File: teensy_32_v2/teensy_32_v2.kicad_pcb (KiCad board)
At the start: 4 copper layers, 65 x 56.5 mm, 5 parts, among them P1 S9200-ND

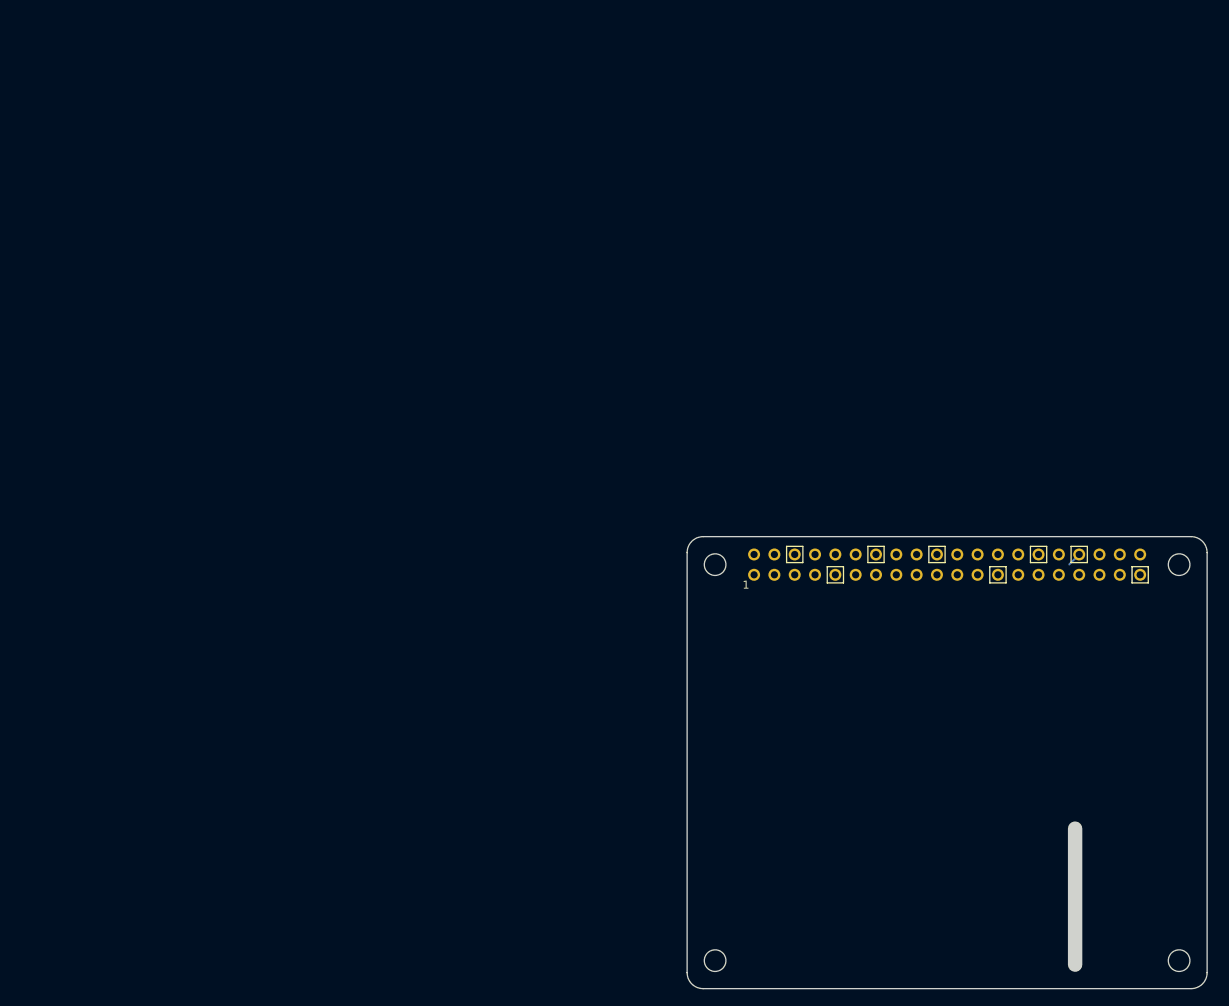
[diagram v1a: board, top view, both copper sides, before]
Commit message: another attempt at Hat layout -- pre routing
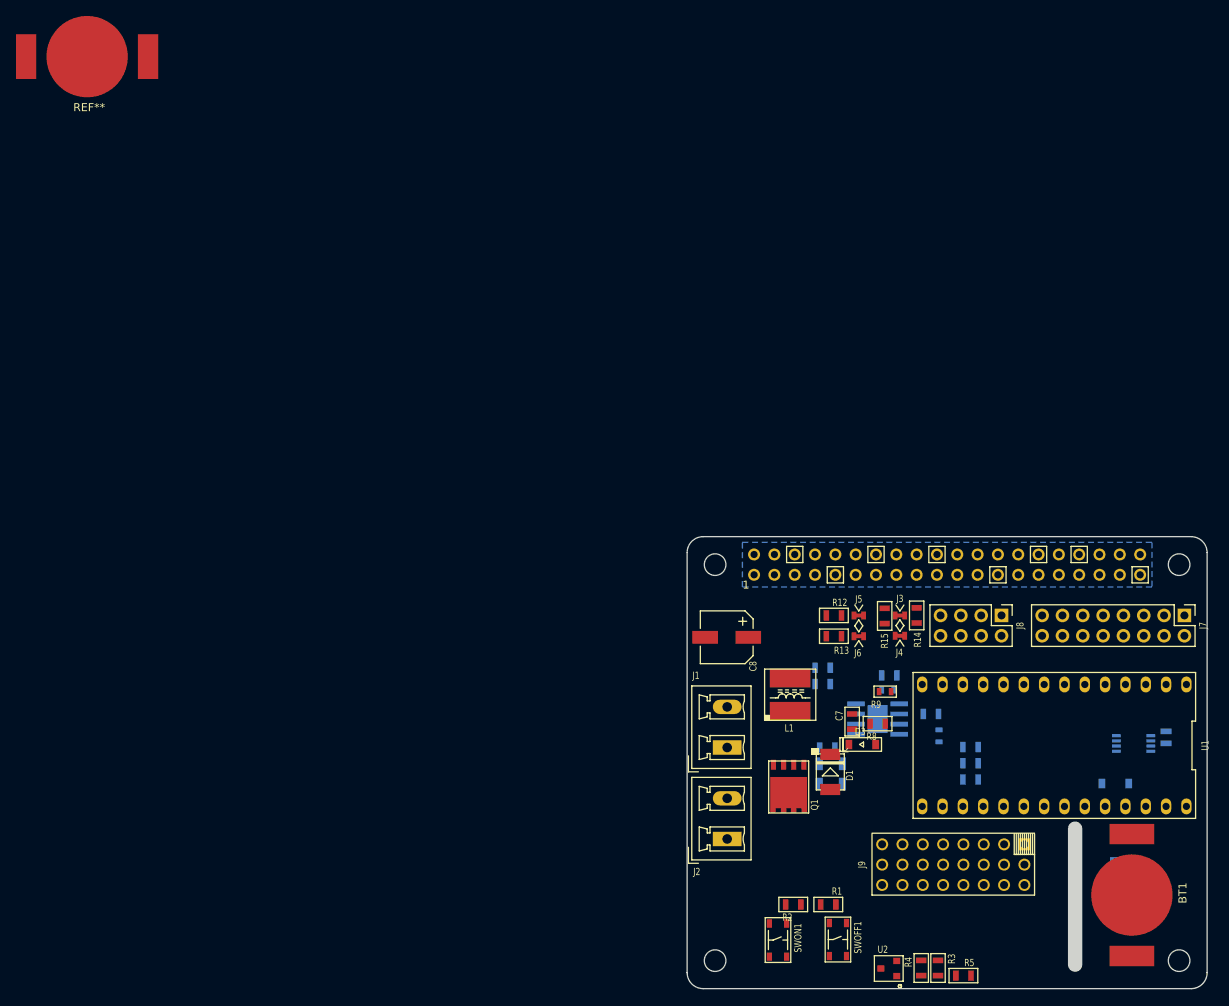
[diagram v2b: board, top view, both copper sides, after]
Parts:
- added BT1: BC-2009-ND, teensy:BC-2009-ND, F.Cu at (130.6, 104.8)
- added C1: MF-CAP-0805-0.1uF, MF_Passives:MF_Passives-C0805, B.Cu at (110.4, 88.3)
- added C10: CL21A226KOQNNNE, MF_Passives:MF_Passives-C0805, B.Cu at (91.9, 76.4)
- added C2: MF-CAP-0805-0.1uF, MF_Passives:MF_Passives-C0805, B.Cu at (92.5, 86.4)
- added C3: CL31A106MBHNNNE, MF_Passives:MF_Passives-C1206, B.Cu at (93.0, 90.9)
- added C4: CL31A106MBHNNNE, MF_Passives:MF_Passives-C1206, B.Cu at (93.0, 88.4)
- added C5: MF-CAP-0805-0.1uF, MF_Passives:MF_Passives-C0805, B.Cu at (100.3, 77.3)
- added C6: MF-CAP-0603-4.7nF, MF_Passives:MF_Passives-C0603, B.Cu at (106.5, 84.9)
- added C7: MF-CAP-0805-0.1uF, MF_Passives:MF_Passives-C0805, F.Cu at (95.6, 83.1)
- added C8: MF-CAP-6.3MM-100uF, MF_Passives:MF_Passives-CP6.3MM, F.Cu at (79.9, 72.6)
- added C9: CL21A226KOQNNNE, MF_Passives:MF_Passives-C0805, B.Cu at (91.9, 78.4)
- added D1: PMEG3050EP,115, teensy:SOD-128, F.Cu at (92.9, 89.4)
- added D2: BAT42, MF_Discrete_Semiconductor:MF_Discrete_Semiconductor-SOD-123, B.Cu at (128.5, 90.9)
- added D3: MF-DIO-SOD123-BAT42, MF_Discrete_Semiconductor:MF_Discrete_Semiconductor-SOD-123, F.Cu at (96.9, 86.0)
- added D4: BAT42, MF_Discrete_Semiconductor:MF_Discrete_Semiconductor-SOD-123, B.Cu at (128.5, 98.8)
- added J1: 277-1667-ND, Connectors_Phoenix:PhoenixContact_MCV-G_02x5.08mm_Vertical, F.Cu at (80.0, 86.4)
- added J2: 277-1667-ND, Connectors_Phoenix:PhoenixContact_MCV-G_02x5.08mm_Vertical, F.Cu at (80.0, 97.8)
- added J3: CJ, teensy:CJ-2, F.Cu at (101.6, 69.8)
- added J4: CJ, teensy:CJ-2, F.Cu at (101.6, 72.4)
- added J5: CJ, teensy:CJ-2, F.Cu at (96.5, 69.8)
- added J6: CJ, teensy:CJ-2, F.Cu at (96.5, 72.5)
- added J7: M20-9980845, Pin_Headers:Pin_Header_Straight_2x08_Pitch2.54mm, F.Cu at (137.2, 69.8)
- added J8: M20-9970445, Pin_Headers:Pin_Header_Straight_2x04_Pitch2.54mm, F.Cu at (114.3, 69.8)
- added J9: Drive, teensy:CONN_03x08, F.Cu at (107.0, 101.0)
- added L1: SRN6045TA-6R3M, teensy:SRN6045TA, F.Cu at (87.9, 79.8)
- added Q1: STL62P3LLH6, teensy:POWERFLAT_5x6, F.Cu at (87.7, 90.0)
- added R1: MF-RES-0805-15K, MF_Passives:MF_Passives-R0805, F.Cu at (92.6, 106.0)
- added R10: RC0603FR-0712KL, MF_Passives:MF_Passives-R0603, B.Cu at (100.1, 79.2)
- added R12: MF-RES-0603-2K, MF_Passives:MF_Passives-R0805, F.Cu at (93.3, 69.8)
- added R13: MF-RES-0603-2K, MF_Passives:MF_Passives-R0805, F.Cu at (93.3, 72.5)
- added R14: MF-RES-0603-2K, MF_Passives:MF_Passives-R0805, F.Cu at (103.7, 69.8)
- added R15: MF-RES-0603-2K, MF_Passives:MF_Passives-R0805, F.Cu at (99.7, 69.9)
- added R16: MF-RES-0805-15K, MF_Passives:MF_Passives-R0805, B.Cu at (105.5, 82.2)
- added R2: MF-RES-0604-2K, MF_Passives:MF_Passives-R0805, F.Cu at (88.3, 106.0)
- added R3: MF-RES-0805-100K, MF_Passives:MF_Passives-R0805, F.Cu at (106.4, 113.9)
- added R4: MF-RES-0805-100K, MF_Passives:MF_Passives-R0805, F.Cu at (104.3, 113.9)
- added R5: MF-RES-0604-2K, MF_Passives:MF_Passives-R0805, F.Cu at (109.5, 114.9)
- added R6: MF-RES-0805-470K, MF_Passives:MF_Passives-R0805, B.Cu at (110.4, 90.4)
- added R7: MF-RES-0805-100K, MF_Passives:MF_Passives-R0805, B.Cu at (110.4, 86.3)
- added R8: MF-RES-0805-100K, MF_Passives:MF_Passives-R0805, F.Cu at (98.8, 83.4)
- added R9: RC0603FR-0763K4L, MF_Passives:MF_Passives-R0603, F.Cu at (99.8, 79.4)
- added REF**: BC-2009-ND, BC-2009-ND, F.Cu at (0.00, 0.00)
- added SWOFF1: MF-SW-TACT-4.2MM, MF_Switches:MF_Switches-TACT4.2MM, F.Cu at (93.9, 110.4)
- added SWON1: MF-SW-TACT-4.2MM, MF_Switches:MF_Switches-TACT4.2MM, F.Cu at (86.4, 110.4)
- added U1: TEENSY_3, teensy:TEENSY_3, F.Cu at (120.9, 86.1)
- added U2: MF-DSC-SOT233-BSS138, MF_Discrete_Semiconductor:MF_Discrete_Semiconductor-SOT-23-3, F.Cu at (100.2, 114.0)
- added U3: DS7257G, teensy:DS7257G, B.Cu at (98.8, 82.8)
- added U4: PCF8563TS/5,118, Housings_SSOP:TSSOP-8_3x3mm_Pitch0.65mm, B.Cu at (130.8, 85.9)
- added Y1: 32 kHz, teensy:SC-20S, B.Cu at (134.9, 85.1)
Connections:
- net +2V5 renamed +3V3
- net /R_12 renamed Net-(P1-Pad32)
- net /R_13 renamed Net-(P1-Pad33)
- net /R_16 renamed Net-(P1-Pad36)
- net /R_17 renamed Net-(P1-Pad11)
- net /R_18 renamed Net-(P1-Pad12)
- net /R_19 renamed Net-(P1-Pad35)
- net /R_20 renamed Net-(P1-Pad38)
- net /R_21 renamed Net-(P1-Pad40)
- net /R_22 renamed Net-(P1-Pad15)
- net /R_23 renamed Net-(P1-Pad16)
- net /R_24 renamed Net-(P1-Pad18)
- net /R_25 renamed Net-(P1-Pad22)
- net /R_26 renamed Net-(P1-Pad37)
- net /R_27 renamed Net-(P1-Pad13)
- net /R_4 renamed Net-(P1-Pad7)
- net /R_5 renamed Net-(P1-Pad29)
- net /R_6 renamed Net-(P1-Pad31)
- net /R_CE0 renamed Net-(P1-Pad24)
- net /R_CE1 renamed Net-(P1-Pad26)
- net /R_ID_SC renamed Net-(P1-Pad28)
- net /R_ID_SD renamed Net-(P1-Pad27)
- net /R_MISO renamed Net-(P1-Pad21)
- net /R_MOSI renamed Net-(P1-Pad19)
- net /R_SCK renamed Net-(P1-Pad23)
- P1 pad 10: /R_RXD -> /R_RX
- P1 pad 8: /R_TXD -> /R_TX
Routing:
- net GND: track 1.90 -> 0.00 mm
- added copper zone on B.Cu, net GND
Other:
- copper layers 4 -> 2
- net class Default: clearance 0.2 -> 0.13
- rule trace_clearance: 0.2 -> 0.13

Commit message: Macrofab proto order of teensy hat v2b
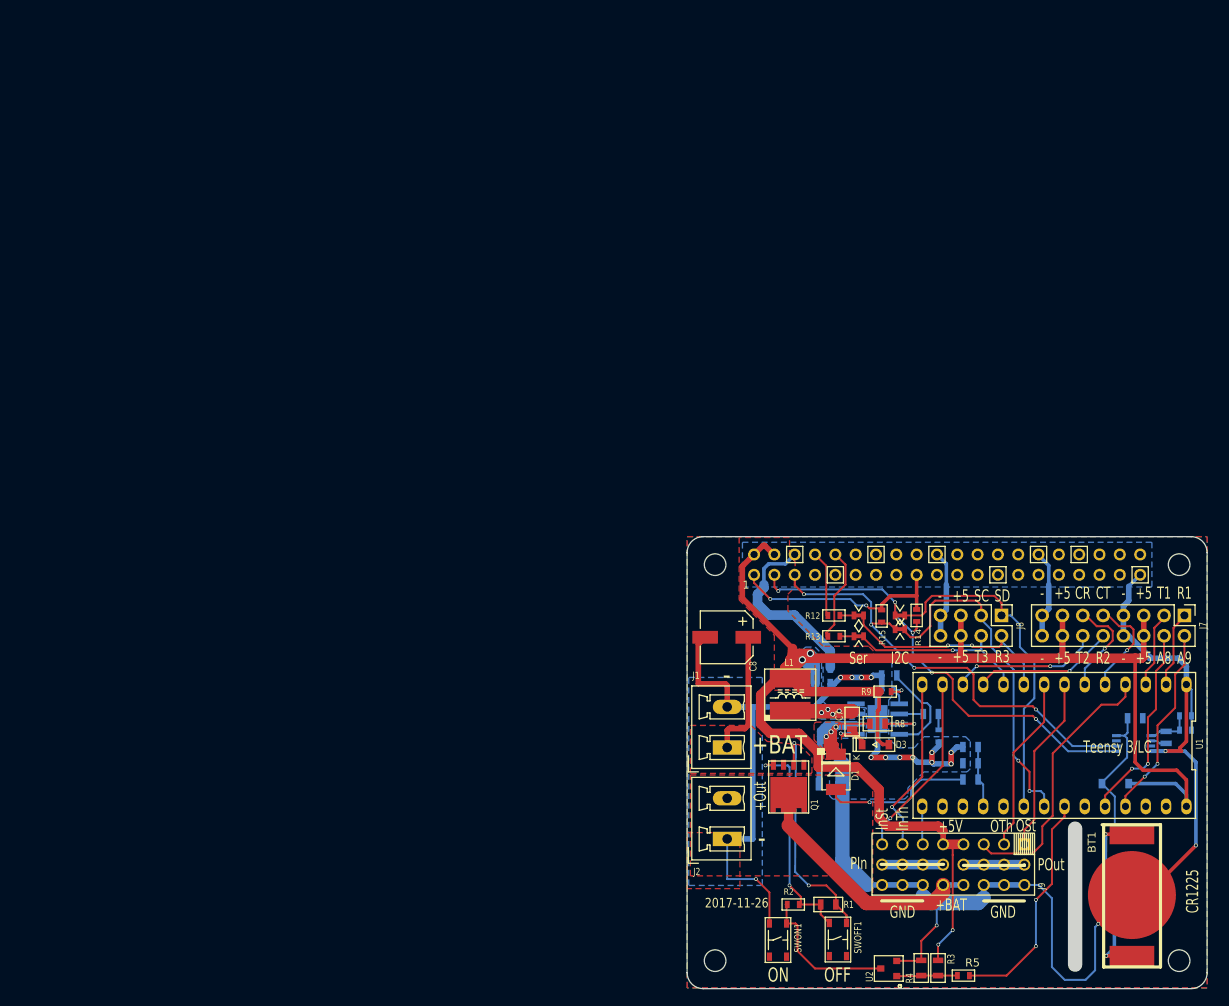
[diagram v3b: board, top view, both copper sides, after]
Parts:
- removed the REF** at (0.00, 0.00)
- added C11: MF-CAP-0805-0.1uF, MF_Passives:MF_Passives-C0805, B.Cu at (131.0, 82.7)
- added C12: MF-CAP-0603-4.7nF, MF_Passives:MF_Passives-C0603, B.Cu at (137.3, 82.4)
- added C13: MF-CAP-0603-4.7nF, MF_Passives:MF_Passives-C0603, B.Cu at (137.3, 84.2)
- R12, R13, R14, R15: footprint MF_Passives:MF_Passives-R0805 -> MF_Passives:MF_Passives-R0603
- R2, R5: value MF-RES-0604-2K -> MF-RES-0603-2K; footprint MF_Passives:MF_Passives-R0805 -> MF_Passives:MF_Passives-R0603
- Y1: value 32 kHz -> SC20S-12.5PF20PPM
- moved D3 1.65 mm to (98.6, 86.0)
- moved J4 0.83 mm to (101.6, 71.6)
- moved D1 0.70 mm to (93.6, 89.4)
- moved R15 0.38 mm to (99.3, 69.9)
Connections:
- net +BATT renamed +12V
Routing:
- net GND: track 0.00 -> 300.2 mm, vias 0 -> 17
- net +5V: track 0.00 -> 214.6 mm, vias 0 -> 4
- net /R_SDA: track 0.00 -> 60.0 mm, vias 0 -> 5
- net /R_SCL: track 0.00 -> 56.7 mm, vias 0 -> 4
- net +12V: track 0.00 -> 50.3 mm, vias 0 -> 1
- net /Power/VIN: track 0.00 -> 45.3 mm, vias 0 -> 2
- net /T_SCL: track 0.00 -> 43.0 mm, vias 0 -> 2
- net /T_SDA: track 0.00 -> 42.5 mm
- net /Power/V_SW: track 0.00 -> 41.8 mm, vias 0 -> 4
- net /Power/V_VIN: track 0.00 -> 34.5 mm, vias 0 -> 3
- net /OUT_AUX: track 0.00 -> 33.8 mm
- net /PWR_CTL: track 0.00 -> 28.6 mm, vias 0 -> 2
- net /T_RX3: track 0.00 -> 28.2 mm, vias 0 -> 2
- net +3V3: track 0.00 -> 27.7 mm, vias 0 -> 2
- net Net-(Q1-Pad2): track 0.00 -> 27.1 mm, vias 0 -> 2
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- added copper zone on F.Cu, net +12V
- added copper zone on B.Cu, net +5V
- added copper zone on F.Cu, net +5V
- added copper zone on F.Cu, net /Power/VIN
- added copper zone on B.Cu, net /Power/V_SW
- added copper zone on F.Cu, net /Power/V_VIN
- added copper zone on F.Cu, net GND
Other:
- net class Default: via_drill 0.305 -> 0.31
- rule via_min_drill: 0.305 -> 0.31
- board text added: "+5"
- board text added: "+5V"
- board text added: "+BAT"
- board text added: "+IN"
- board text added: "+OUT"
- board text added: "+Out"
- board text added: "-"
- board text added: "13"
- board text added: "14"
- board text added: "15"
- board text added: "2017-11-26"
- board text added: "4"
- board text added: "7"
- board text added: "8"
- board text added: "A8"
- board text added: "A9"
- board text added: "CR"
- board text added: "CR1225"
- board text added: "CT"
- board text added: "GND"
- board text added: "I2C"
- board text added: "InSt"
- board text added: "InTh"
- board text added: "OFF"
- board text added: "ON"
- board text added: "OSt"
- board text added: "OTh"
- board text added: "PIn"
- board text added: "POut"
- board text added: "R1"
- board text added: "R2"
- board text added: "R3"
- board text added: "SC"
- board text added: "SD"
- board text added: "Ser"
- board text added: "T1"
- board text added: "T2"
- board text added: "T3"
- board text added: "Teensy 3/LC"
- board text added: "Teensy Hat for Donkey Car github.com/jwatte/donkey_racing 2017-11-26"

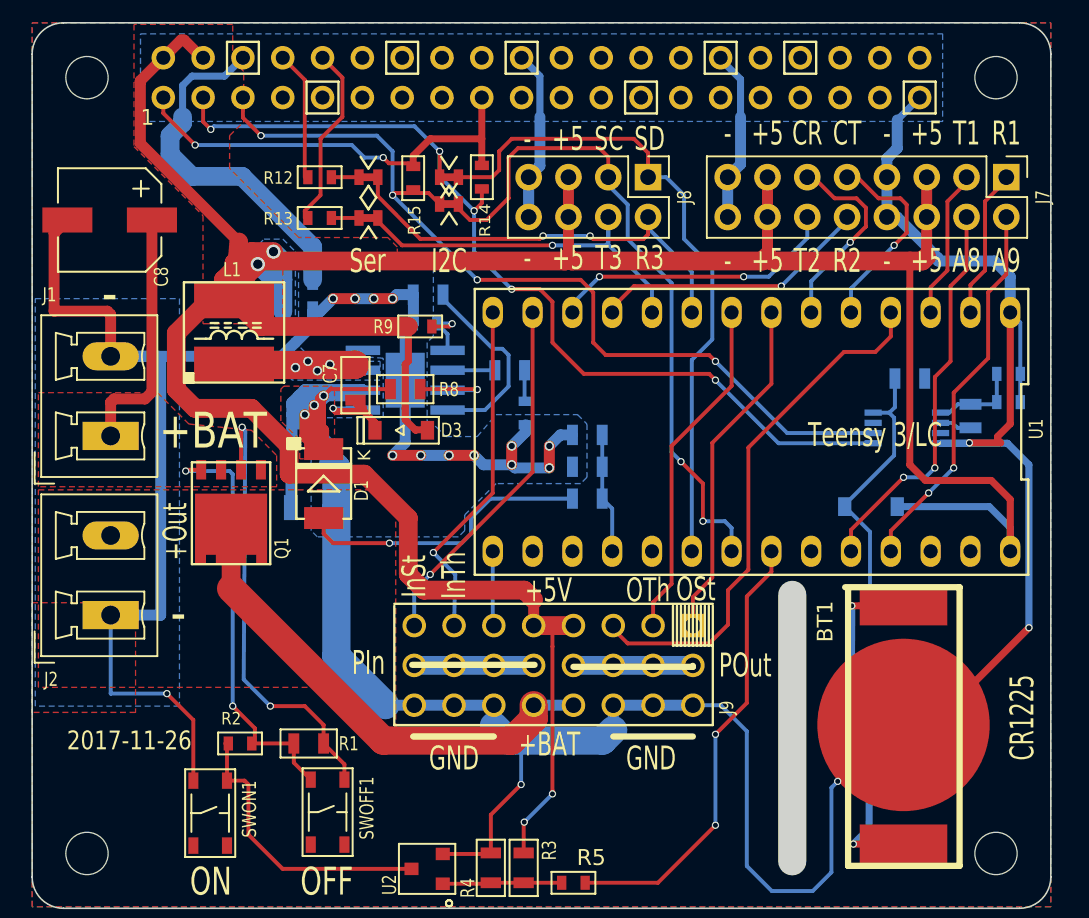
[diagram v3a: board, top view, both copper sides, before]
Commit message: update teensy hat schematic
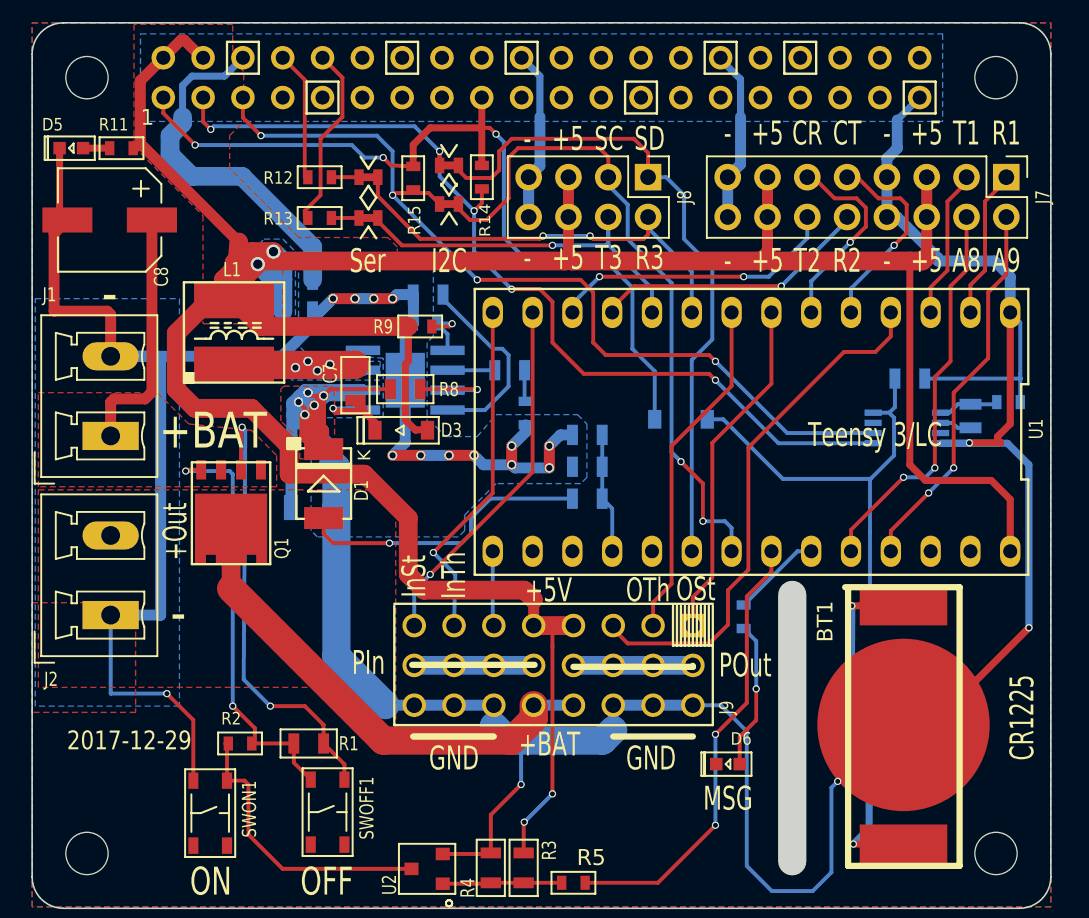
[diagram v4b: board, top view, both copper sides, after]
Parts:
- removed C12: MF-CAP-0603-4.7nF, MF_Passives:MF_Passives-C0603
- added D5: MF-LED-0603-GREEN, MF_LEDs:MF_LEDs-LED0603, F.Cu at (77.5, 68.0)
- added D6: MF-LED-0603-RED, MF_LEDs:MF_LEDs-LED0603, F.Cu at (119.4, 107.3)
- added R11: MF-RES-0603-2K, MF_Passives:MF_Passives-R0603, F.Cu at (80.7, 68.0)
- added R17: MF-RES-0603-2K, MF_Passives:MF_Passives-R0603, B.Cu at (120.4, 97.9)
- C13: value MF-CAP-0603-4.7nF -> MF-CAP-0402-8.2pF
- D1: value PMEG3050EP,115 -> PMEG3050BEP,115
- J9: value Drive -> TSW-108-07-G-T
- U1: value TEENSY_3 -> TEENSY
- U3: value DS7257G -> RT7257G
- moved D2 13.3 mm to (116.4, 85.3), turned to 180 degrees
- moved J3 0.75 mm to (101.6, 69.1)
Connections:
- D2 pad ANOD: +5V -> +3V3
- U1 pad 23: Net-(U1-Pad23) -> /MSG_LED
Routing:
- net +3V3: track 27.7 -> 55.2 mm, vias 2 -> 3
- net GND: track 300.2 -> 311.2 mm
- net Net-(C11-Pad1): track 17.7 -> 28.6 mm
- net Net-(D6-PadANOD): track 0.00 -> 9.42 mm, vias 0 -> 1
- net +5V: track 214.6 -> 206.1 mm
- net /MSG_LED: track 0.00 -> 5.78 mm
- net /Power/V_VIN: track 34.5 -> 37.4 mm, vias 3 -> 5
- net Net-(C13-Pad1): track 5.67 -> 3.87 mm
- net Net-(D5-PadANOD): track 0.00 -> 1.70 mm
- net /R_SDA: track 60.0 -> 59.2 mm
- net /T_SDA: track 42.5 -> 43.1 mm
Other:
- board text added: "2017-12-29"
- board text added: "MSG"
- board text added: "Teensy Hat for Donkey Car github.com/jwatte/donkey_racing 2017-12-29"
- board text removed: "2017-11-26"
- board text removed: "Teensy Hat for Donkey Car github.com/jwatte/donkey_racing 2017-11-26"

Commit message: version 2017-12-30 of hat
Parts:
- added D7: ESD9M5.0ST5G, teensy:SOD-923, B.Cu at (138.1, 91.8)
- moved C5 9.19 mm to (104.3, 85.6), turned to 270 degrees
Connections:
- J7 pad 1: /T_RX1 -> /T_TX1
- J7 pad 10: /T_RX2 -> /T_TX2
- J7 pad 12: /T_TX2 -> /T_RX2
- J7 pad 3: /T_TX1 -> /T_RX1
- J8 pad 2: /T_RX3 -> /T_TX3
- J8 pad 4: /T_TX3 -> /T_RX3
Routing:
- net /Power/V_SS: track 12.5 -> 2.39 mm
- net /T_SCL: track 43.0 -> 49.7 mm, vias 2 -> 0
- net GND: track 311.2 -> 317.7 mm
- net /T_TX1: track 9.58 -> 12.1 mm, vias 0 -> 1
- net +12V: track 50.3 -> 47.9 mm
- net +5V: track 206.1 -> 208.3 mm
- net /T_RX2: track 17.8 -> 15.6 mm
- net /T_TX2: track 18.6 -> 20.5 mm
- net /T_SDA: track 43.1 -> 42.2 mm
- net /T_RX3: track 28.2 -> 28.4 mm, vias 2 -> 3
- net (no net): vias 0 -> 4
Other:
- board text added: "2017-12-30"
- board text added: "POWER"
- board text added: "Teensy Hat for Donkey Car github.com/jwatte/donkey_racing 2017-12-30"
- board text removed: "2017-12-29"
- board text removed: "Teensy Hat for Donkey Car github.com/jwatte/donkey_racing 2017-12-29"
